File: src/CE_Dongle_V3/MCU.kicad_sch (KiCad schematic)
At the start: 42 parts, among them J3 Conn_Coaxial, J4 Conn_02x05_Odd_Even, U1 ESP32-C6, U3 W25Q64JWUUIQ, Y1 40MHz

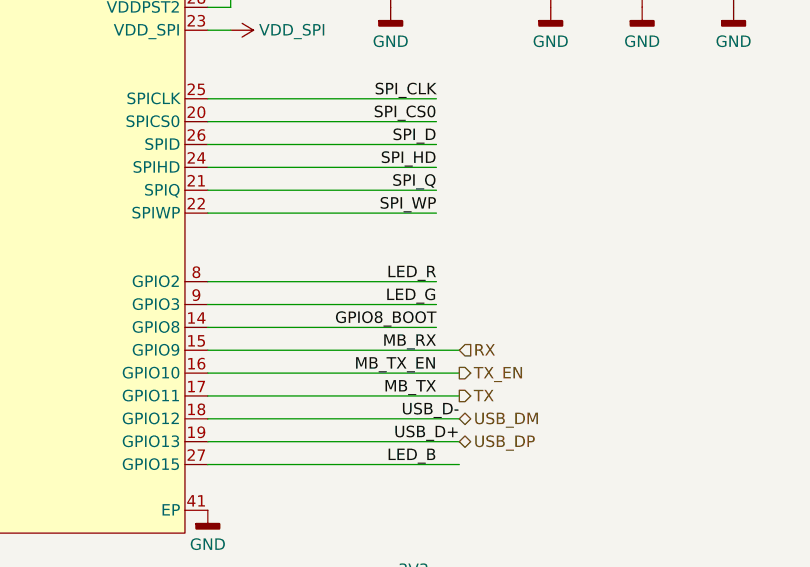
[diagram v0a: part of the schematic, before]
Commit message: layout cont. corrected some wrong net names
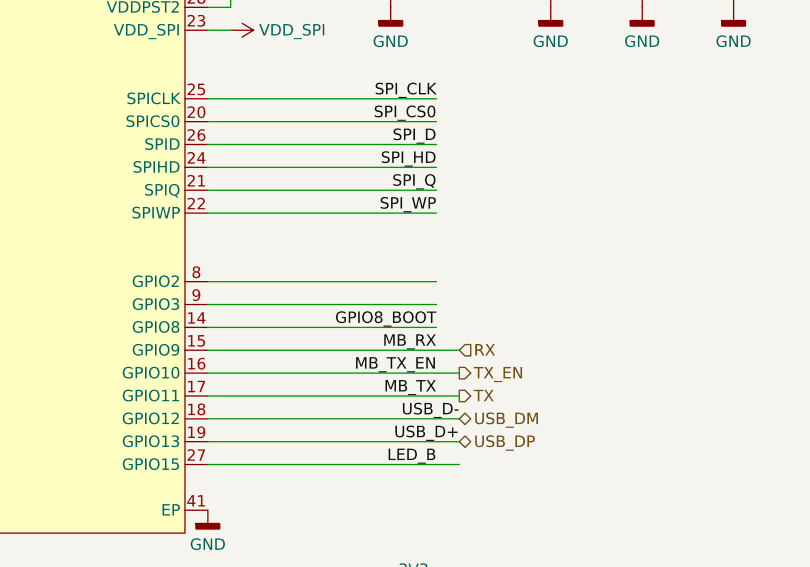
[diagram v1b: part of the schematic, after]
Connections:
- net LED_G: no longer U1.9 (GPIO3)
- net LED_R: no longer U1.8 (GPIO2)
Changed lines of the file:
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@@
-	)
-	(label "LED_R"
-		(at 177.8 96.52 180)
-		(effects
-			(font
-				(size 1.27 1.27)
-			)
-			(justify right bottom)
-		)
 	)
 	(label "LED_R"
@@
 		)
 	)
-	(label "LED_G"
-		(at 177.8 99.06 180)
-		(effects
-			(font
-				(size 1.27 1.27)
-			)
-			(justify right bottom)
-		)
-	)

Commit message: layout finished
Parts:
- R12, R13, R15, R16, R17: value 100R -> 22R; symbol Resistor:0402WGF1000TCE -> Resistor:0402WGF220JTCE; LCSC Part C25076 -> C25092; Manufacturer Part Number 1 0402WGF1000TCE -> 0402WGF220JTCE; Supplier Part Number 1 C25076 -> C25092
- R18: value 0R -> 120R; symbol Resistor:0402WGF0000TCE -> Resistor:0402WGF1200TCE; LCSC Part C17168 -> C25079; Manufacturer Part Number 1 0402WGF0000TCE -> 0402WGF1200TCE; Supplier Part Number 1 C17168 -> C25079
- SW_BOOT1, SW_RST1, SW_USR1: footprint 7Sigma:SW_SPST_6.0mm_6.0mm -> 7Sigma:SW-SMD_4P-L6.0-W6.0-P4.50-LS9.0-H4.3
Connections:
- net BTTN: now also SW_USR1.3 (K), SW_USR1.4 (A); no longer SW_USR1.2
- net GND: now also SW_BOOT1.2, SW_RST1.2, SW_USR1.2
- net GPIO8_BOOT: now also SW_BOOT1.3 (K), SW_BOOT1.4 (A); no longer SW_BOOT1.2
- net RST: now also SW_RST1.3 (K), SW_RST1.4 (A); no longer SW_RST1.2
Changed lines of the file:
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@@
 	)
 	(junction
+		(at 50.8 152.4)
+		(diameter 0)
+		(color 0 0 0 0)
+	)
+	(junction
 		(at 81.28 105.41)
 		(diameter 0)
@@
 	)
 	(junction
+		(at 29.21 152.4)
+		(diameter 0)
+		(color 0 0 0 0)
+	)
+	(junction
 		(at 154.94 63.5)
 		(diameter 0)
@@
 	)
 	(junction
+		(at 68.58 152.4)
+		(diameter 0)
+		(color 0 0 0 0)
+	)
+	(junction
 		(at 226.06 143.51)
 		(diameter 0)
@@
 	(wire
 		(pts
+			(xy 26.67 152.4) (xy 29.21 152.4)
+		)
+		(stroke
+			(width 0)
+			(type default)
+		)
+	)
+	(wire
+		(pts
 			(xy 167.64 142.24) (xy 167.64 139.7)
 		)
@@
 	(wire
 		(pts
+			(xy 48.26 142.24) (xy 50.8 142.24)
+		)
+		(stroke
+			(width 0)
+			(type default)
+		)
+	)
+	(wire
+		(pts
 			(xy 175.26 144.78) (xy 175.26 139.7)
 		)
@@
 	(wire
 		(pts
+			(xy 48.26 152.4) (xy 50.8 152.4)
+		)
+		(stroke
+			(width 0)
+			(type default)
+		)
+	)
+	(wire
+		(pts
 			(xy 99.06 119.38) (xy 114.3 119.38)
 		)
@@
 	(wire
 		(pts
+			(xy 66.04 152.4) (xy 68.58 152.4)
+		)
+		(stroke
+			(width 0)
+			(type default)
+		)
+	)
+	(wire
+		(pts
 			(xy 101.6 83.82) (xy 114.3 83.82)
 		)
@@
 	(wire
 		(pts
+			(xy 66.04 142.24) (xy 68.58 142.24)
+		)
+		(stroke
+			(width 0)
+			(type default)
+		)
+	)
+	(wire
+		(pts
 			(xy 152.4 96.52) (xy 177.8 96.52)
 		)
@@
 	(wire
 		(pts
+			(xy 26.67 142.24) (xy 29.21 142.24)
+		)
+		(stroke
+			(width 0)
+			(type default)
+		)
+	)
+	(wire
+		(pts
 			(xy 68.58 137.16) (xy 68.58 142.24)
 		)
@@
 		(dnp no)
 		(property "Reference" "SW_BOOT1"
-			(at 66.04 146.05 0)
+			(at 70.104 152.654 0)
 			(effects
 				(font
@@
 			)
 		)
-		(property "Footprint" "7Sigma:SW_SPST_6.0mm_6.0mm"
+		(property "Footprint" "7Sigma:SW-SMD_4P-L6.0-W6.0-P4.50-LS9.0-H4.3"
 			(at 63.5 147.32 0)
 			(effects
@@
 		(pin "1"
 		)
+		(pin "4"
+		)
+		(pin "3"
+		)
 		(instances
 			(project "CE_Dongle_V3"
@@
 	)
 	(symbol
-		(lib_id "Resistor:0402WGF1000TCE")
+		(lib_id "Resistor:0402WGF220JTCE")
 		(at 222.25 156.21 90)
 		(unit 1)
@@
 			)
 		)
-		(property "Value" "100R"
+		(property "Value" "22R"
 			(at 226.568 154.94 90)
 			(do_not_autoplace yes)
@@
 			)
 		)
-		(property "Datasheet" "https://www.lcsc.com/datasheet/C25076.pdf"
+		(property "Datasheet" "https://atta.szlcsc.com/upload/public/pdf/source/20200306/C422600_1E6D84923E4A46A82E41ADD87F860B5C.pdf"
 			(at 222.25 156.21 0)
 			(effects
@@
 			)
 		)
-		(property "Description" "100R 63mW 1% 0402"
+		(property "Description" "22R 63mW 1% 0402"
 			(at 222.25 156.21 0)
 			(effects
@@
 			)
 		)
-		(property "Manufacturer Part Number 1" "0402WGF1000TCE"
+		(property "Manufacturer Part Number 1" "0402WGF220JTCE"
 			(at 222.25 156.21 0)
 			(effects
@@
 			)
 		)
-		(property "Supplier Part Number 1" "C25076"
+		(property "Supplier Part Number 1" "C25092"
 			(at 222.25 156.21 0)
 			(effects
@@
 			)
 		)
-		(property "LCSC Part" "C25076"
+		(property "LCSC Part" "C25092"
 			(at 222.25 156.21 0)
 			(effects
@@
 	)
 	(symbol
-		(lib_id "Resistor:0402WGF1000TCE")
+		(lib_id "Resistor:0402WGF220JTCE")
 		(at 222.25 148.59 90)
 		(unit 1)
@@
 			)
 		)
-		(property "Value" "100R"
+		(property "Value" "22R"
 			(at 226.568 147.32 90)
 			(do_not_autoplace yes)
@@
 			)
 		)
-		(property "Datasheet" "https://www.lcsc.com/datasheet/C25076.pdf"
+		(property "Datasheet" "https://atta.szlcsc.com/upload/public/pdf/source/20200306/C422600_1E6D84923E4A46A82E41ADD87F860B5C.pdf"
 			(at 222.25 148.59 0)
 			(effects
@@
 			)
 		)
-		(property "Description" "100R 63mW 1% 0402"
+		(property "Description" "22R 63mW 1% 0402"
 			(at 222.25 148.59 0)
 			(effects
@@
 			)
 		)
-		(property "Manufacturer Part Number 1" "0402WGF1000TCE"
+		(property "Manufacturer Part Number 1" "0402WGF220JTCE"
 			(at 222.25 148.59 0)
 			(effects
@@
 			)
 		)
-		(property "Supplier Part Number 1" "C25076"
+		(property "Supplier Part Number 1" "C25092"
 			(at 222.25 148.59 0)
 			(effects
@@
 			)
 		)
-		(property "LCSC Part" "C25076"
+		(property "LCSC Part" "C25092"
 			(at 222.25 148.59 0)
 			(effects
@@
 	)
 	(symbol
-		(lib_id "Resistor:0402WGF1000TCE")
+		(lib_id "Resistor:0402WGF220JTCE")
 		(at 222.25 146.05 90)
 		(unit 1)
@@
 			)
 		)
-		(property "Value" "100R"
+		(property "Value" "22R"
 			(at 226.568 144.78 90)
 			(do_not_autoplace yes)
@@
 			)
 		)
-		(property "Datasheet" "https://www.lcsc.com/datasheet/C25076.pdf"
+		(property "Datasheet" "https://atta.szlcsc.com/upload/public/pdf/source/20200306/C422600_1E6D84923E4A46A82E41ADD87F860B5C.pdf"
 			(at 222.25 146.05 0)
 			(effects
@@
 			)
 		)
-		(property "Description" "100R 63mW 1% 0402"
+		(property "Description" "22R 63mW 1% 0402"
 			(at 222.25 146.05 0)
 			(effects
@@
 			)
 		)
-		(property "Manufacturer Part Number 1" "0402WGF1000TCE"
+		(property "Manufacturer Part Number 1" "0402WGF220JTCE"
 			(at 222.25 146.05 0)
 			(effects
@@
 			)
 		)
-		(property "Supplier Part Number 1" "C25076"
+		(property "Supplier Part Number 1" "C25092"
 			(at 222.25 146.05 0)
 			(effects
@@
 			)
 		)
-		(property "LCSC Part" "C25076"
+		(property "LCSC Part" "C25092"
 			(at 222.25 146.05 0)
 			(effects
@@
 		(dnp no)
 		(property "Reference" "SW_RST1"
-			(at 48.26 146.05 0)
+			(at 52.578 151.638 0)
 			(effects
 				(font
@@
 			)
 		)
-		(property "Footprint" "7Sigma:SW_SPST_6.0mm_6.0mm"
+		(property "Footprint" "7Sigma:SW-SMD_4P-L6.0-W6.0-P4.50-LS9.0-H4.3"
 			(at 45.72 147.32 0)
 			(effects
@@
 		(pin "1"
 		)
+		(pin "4"
+		)
+		(pin "3"
+		)
 		(instances
 			(project ""
@@
 	)
 	(symbol
-		(lib_id "Resistor:0402WGF1000TCE")
+		(lib_id "Resistor:0402WGF220JTCE")
 		(at 222.25 151.13 90)
 		(unit 1)
@@
 			)
 		)
-		(property "Value" "100R"
+		(property "Value" "22R"
 			(at 226.568 149.86 90)
 			(do_not_autoplace yes)
@@
 			)
 		)
-		(property "Datasheet" "https://www.lcsc.com/datasheet/C25076.pdf"
+		(property "Datasheet" "https://atta.szlcsc.com/upload/public/pdf/source/20200306/C422600_1E6D84923E4A46A82E41ADD87F860B5C.pdf"
 			(at 222.25 151.13 0)
 			(effects
@@
 			)
 		)
-		(property "Description" "100R 63mW 1% 0402"
+		(property "Description" "22R 63mW 1% 0402"
 			(at 222.25 151.13 0)
 			(effects
@@
 			)
 		)
-		(property "Manufacturer Part Number 1" "0402WGF1000TCE"
+		(property "Manufacturer Part Number 1" "0402WGF220JTCE"
 			(at 222.25 151.13 0)
 			(effects
@@
 			)
 		)
-		(property "Supplier Part Number 1" "C25076"
+		(property "Supplier Part Number 1" "C25092"
 			(at 222.25 151.13 0)
 			(effects
@@
 			)
 		)
-		(property "LCSC Part" "C25076"
+		(property "LCSC Part" "C25092"
 			(at 222.25 151.13 0)
 			(effects
@@
 		(dnp no)
 		(property "Reference" "SW_USR1"
-			(at 26.67 146.05 0)
+			(at 30.734 152.146 0)
 			(effects
 				(font
@@
 			)
 		)
-		(property "Footprint" "7Sigma:SW_SPST_6.0mm_6.0mm"
+		(property "Footprint" "7Sigma:SW-SMD_4P-L6.0-W6.0-P4.50-LS9.0-H4.3"
 			(at 24.13 147.32 0)
 			(effects
@@
 		(pin "1"
 		)
+		(pin "4"
+		)
+		(pin "3"
+		)
 		(instances
 			(project "CE_Dongle_V3"
@@
 	)
 	(symbol
-		(lib_id "Resistor:0402WGF0000TCE")
+		(lib_id "Resistor:0402WGF1200TCE")
 		(at 100.33 99.06 90)
 		(unit 1)
@@
 			)
 		)
-		(property "Value" "0R"
+		(property "Value" "120R"
 			(at 100.33 100.584 90)
 			(do_not_autoplace yes)
@@
 			)
 		)
-		(property "Datasheet" "https://www.lcsc.com/datasheet/C17168.pdf"
+		(property "Datasheet" "https://atta.szlcsc.com/upload/public/pdf/source/20200306/C422600_1E6D84923E4A46A82E41ADD87F860B5C.pdf"
 			(at 100.33 99.06 0)
 			(effects
@@
 			)
 		)
-		(property "Description" "0R 63mW 1% 0402"
+		(property "Description" "120R 63mW 1% 0402"
 			(at 100.33 99.06 0)
 			(effects
@@
 			)
 		)
-		(property "Manufacturer Part Number 1" "0402WGF0000TCE"
+		(property "Manufacturer Part Number 1" "0402WGF1200TCE"
 			(at 100.33 99.06 0)
 			(effects
@@
 			)
 		)
-		(property "Supplier Part Number 1" "C17168"
+		(property "Supplier Part Number 1" "C25079"
 			(at 100.33 99.06 0)
 			(effects
@@
 			)
 		)
-		(property "LCSC Part" "C17168"
+		(property "LCSC Part" "C25079"
 			(at 100.33 99.06 0)
 			(effects
@@
 	)
 	(symbol
-		(lib_id "Resistor:0402WGF1000TCE")
+		(lib_id "Resistor:0402WGF220JTCE")
 		(at 222.25 153.67 90)
 		(unit 1)
@@
 			)
 		)
-		(property "Value" "100R"
+		(property "Value" "22R"
 			(at 226.568 152.4 90)
 			(do_not_autoplace yes)
@@
 			)
 		)
-		(property "Datasheet" "https://www.lcsc.com/datasheet/C25076.pdf"
+		(property "Datasheet" "https://atta.szlcsc.com/upload/public/pdf/source/20200306/C422600_1E6D84923E4A46A82E41ADD87F860B5C.pdf"
 			(at 222.25 153.67 0)
 			(effects
@@
 			)
 		)
-		(property "Description" "100R 63mW 1% 0402"
+		(property "Description" "22R 63mW 1% 0402"
 			(at 222.25 153.67 0)
 			(effects
@@
 			)
 		)
-		(property "Manufacturer Part Number 1" "0402WGF1000TCE"
+		(property "Manufacturer Part Number 1" "0402WGF220JTCE"
 			(at 222.25 153.67 0)
 			(effects
@@
 			)
 		)
-		(property "Supplier Part Number 1" "C25076"
+		(property "Supplier Part Number 1" "C25092"
 			(at 222.25 153.67 0)
 			(effects
@@
 			)
 		)
-		(property "LCSC Part" "C25076"
+		(property "LCSC Part" "C25092"
 			(at 222.25 153.67 0)
 			(effects

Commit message: schematic update before production
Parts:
- C14, C15: Supplier 2 (none) -> Mouser; Supplier Part Number 2 (none) -> 81-GJM1555C1H1R2WB1D
- J4: Supplier Part Number 2 None -> (none)
- SW_BOOT1, SW_RST1, SW_USR1: value KH-6X6X4.3H-STM -> KH-6X6X9H-TJ; footprint 7Sigma:SW-SMD_4P-L6.0-W6.0-P4.50-LS9.0-H4.3 -> 7Sigma:SW-TH_4P-L6.0-W6.0-P4.50-LS6.5-H9.0; symbol Buttons:KH-6X6X4.3H-STM -> Buttons:KH-6X6X9H-TJ; LCSC Part C2837530 -> C2837519; Manufacturer Part Number 1 KH-6X6X4.3H-STM -> KH-6X6X9H-TJ; Supplier Part Number 1 C2837530 -> C2837519
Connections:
- no-connect marks 1 -> 6
